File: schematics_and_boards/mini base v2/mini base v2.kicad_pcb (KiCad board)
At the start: 6 copper layers, 24.3 x 24.1 mm, 31 parts, among them J1 Micro Bypass Header, J2 Debug Header, J3 Ext Pwr, U1 BC840, U2 LSM6DSOXTR, U3 OPT4001DTSR, U4 OPT4001DTSR, Y1 32.768KHz

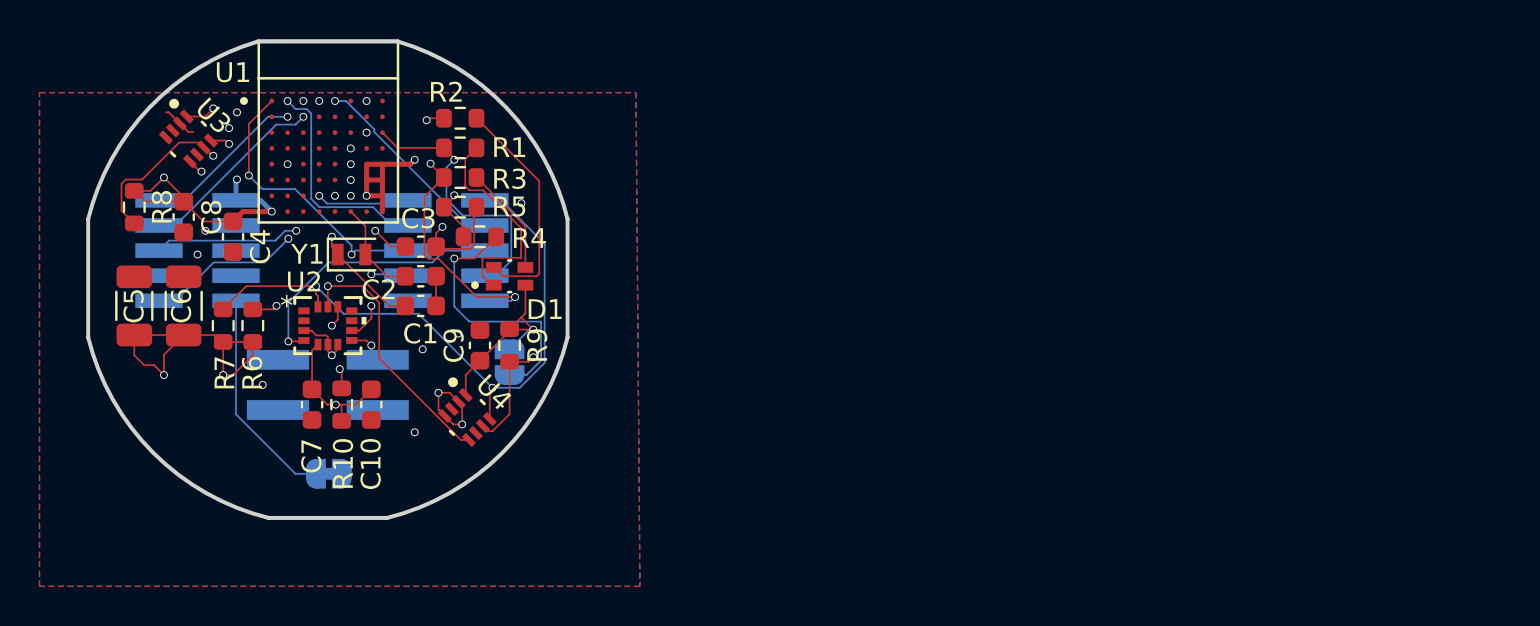
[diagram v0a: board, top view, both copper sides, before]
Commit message: pcb v1 sent for manufacture
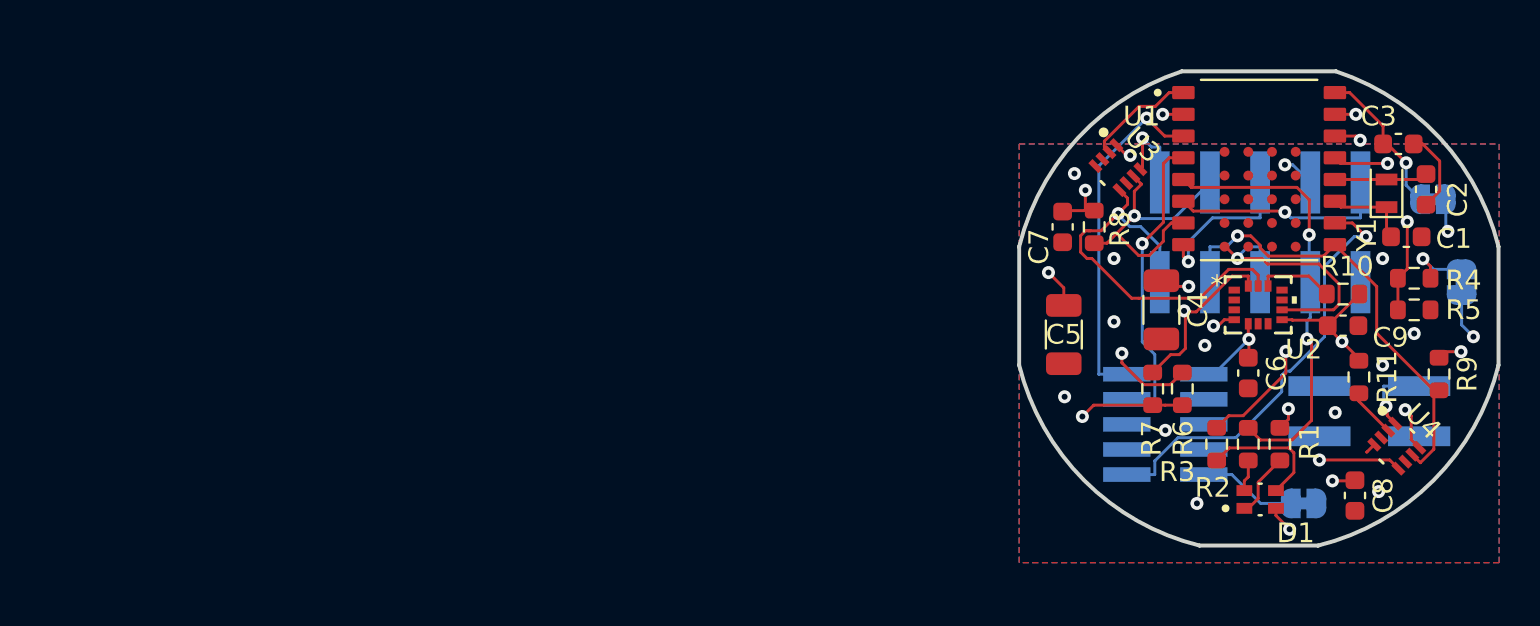
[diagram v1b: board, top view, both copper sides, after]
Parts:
- removed C10: 0.1uF, Capacitor_SMD:C_0603_1608Metric
- added JP3: NRF_DISABLE, Jumper:SolderJumper-2_P1.3mm_Bridged_RoundedPad1.0x1.5mm, B.Cu at (112.8, 36.6)
- added R11: 10k, Resistor_SMD:R_0603_1608Metric, F.Cu at (109.0, 45.6)
- added REF**: Tab, PCM_kikit:Tab, F.Cu at (91.6, 42.2)
- added REF**: Tab, PCM_kikit:Tab, F.Cu at (103.9, 29.9)
- added REF**: Tab, PCM_kikit:Tab, F.Cu at (116.3, 41.8)
- added REF**: Tab, PCM_kikit:Tab, F.Cu at (103.9, 54.3)
- C4: value 4.7uF -> 100 uF; footprint Capacitor_SMD:C_0603_1608Metric -> Capacitor_SMD:C_1206_3216Metric
- C6: value 100 uF -> 0.1uF; footprint Capacitor_SMD:C_1206_3216Metric -> Capacitor_SMD:C_0603_1608Metric
- J1: footprint Connector_PinHeader_1.27mm:PinHeader_2x05_P1.27mm_Vertical_SMD -> Connector_PinHeader_2.54mm:PinHeader_2x05_P2.54mm_Vertical_SMD
- U1: value BC840 -> BC832; footprint anichno:MODULE_BC840 -> anichno:BC832
- moved C8 61.0 mm to (108.8, 51.6)
- moved C6 54.0 mm to (103.4, 45.4), turned to -90 degrees
- moved J3 52.7 mm to (109.5, 47.3)
- moved Y1 52.5 mm to (110.4, 36.3), turned to 90 degrees
- moved C2 51.1 mm to (112.4, 36.1), turned to 90 degrees
- moved R10 51.0 mm to (108.2, 41.4), turned to 180 degrees
- moved C1 50.0 mm to (111.4, 38.5)
- moved J2 49.8 mm to (99.2, 48.0)
- moved C3 49.8 mm to (111.0, 33.8)
- moved JP1 49.4 mm to (106.2, 52.0)
- moved R8 48.6 mm to (95.6, 38.0)
- moved R5 48.6 mm to (111.8, 42.2)
- moved JP2 48.4 mm to (114.2, 40.8), turned to -90 degrees
- moved R4 47.3 mm to (111.8, 40.6)
- moved R6 47.2 mm to (100.1, 46.2)
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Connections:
- C1 pad 2: Net-(U1-P0.00/XL1) -> Net-(U1-P00/XL1)
- C2 pad 2: Net-(U1-P0.01/XL2) -> Net-(U1-P01/XL2)
- C3 pad 1: +3.3V -> Net-(JP3-A)
- J2 pad 6: SWO -> unconnected-(J2-Pin_6-Pad6)
- U1 pad A5: unconnected-(U1-D--PadA5) -> IMU_INT2
- U1 pad B1: SWDIO -> unconnected-(U1-P25-PadB1)
- U1 pad B4: RESET -> unconnected-(U1-P05-PadB4)
- U1 pad C1: SWDCLK -> unconnected-(U1-P24-PadC1)
- U4 pad 2: GND -> Net-(U4-ADDR)
- Y1 pad 1: Net-(U1-P0.00/XL1) -> Net-(U1-P00/XL1)
- Y1 pad 2: Net-(U1-P0.01/XL2) -> Net-(U1-P01/XL2)
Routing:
- net SCL: track 34.1 -> 63.9 mm
- net +3.3V: track 53.0 -> 36.0 mm, vias 11 -> 13
- net SWO: track 14.4 -> 0.00 mm, vias 2 -> 0
- net GND: track 24.4 -> 10.4 mm, vias 17 -> 12
- net IMU_INT1: track 26.6 -> 12.9 mm
- net OPT4001_INT2: track 35.4 -> 23.3 mm, vias 2 -> 1
- net OPT4001_INT1: track 25.7 -> 14.4 mm, vias 2 -> 1
- net STATUS_LED_R: track 14.0 -> 24.9 mm, vias 1 -> 3
- net RESET: track 11.6 -> 21.9 mm, vias 2 -> 1
- net Net-(JP2-A): track 13.6 -> 3.32 mm
- net Net-(D1-GK): track 11.7 -> 1.61 mm
- net SWDIO: track 8.27 -> 17.6 mm
- net STATUS_LED_G: track 13.7 -> 22.9 mm, vias 3 -> 2
- net Net-(U1-P0.00/XL1): track 8.00 -> 0.00 mm, vias 2 -> 0
- net Net-(JP3-A): track 0.00 -> 7.75 mm, vias 0 -> 1
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- removed copper zone on In3.Cu, net GND
- removed copper zone on In4.Cu, net GND
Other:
- board size 24.3 x 24.1 mm -> 24.3 x 24 mm
- copper layers 6 -> 4
- board text added: "V1"
